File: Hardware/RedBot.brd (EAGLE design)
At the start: 94 x 49.5 mm, 53 parts, among them IC1 FT232RLSSOP, J1 5.5x2.1mm Barrel, J2 AVR_SPI_PRG_6PTH, U1 ATMEGA328P, U2 TB6612FNG, U3 MIC5219 5V, U4 MIC5219 3.3V, X1 USB-B, Y1 16MHz

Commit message: v01 files as sent to protos
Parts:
- removed J1: 5.5x2.1mm Barrel, SparkFun-Connectors:POWER_JACK_SMD
- removed J2: AVR_SPI_PRG_6PTH, SparkFun-Connectors:2X3
- removed X1: USB-B, SparkFun-Connectors:USB-B-PTH
- added JP13: (no value), SparkFun-Connectors:2X3_SMT_POSTS
- added SFE-LOGO1: LOGO-SFENEW, SparkFun-Aesthetics:SFE-NEW-WEBLOGO
- added STANDOFF1, STANDOFF2, STANDOFF3, STANDOFF4: STAND-OFF, SparkFun-Electromechanical:STAND-OFF
- added U$17: OSHW-LOGOS, SparkFun-Aesthetics:OSHW-LOGO-S
- JP3: value STAND-OFF -> 5.5x2.1mm Barrel; device SparkFun-Electromechanical:STAND-OFF -> SparkFun-Connectors:POWER_JACK_SMD
- JP4: value STAND-OFF -> USB-B; device SparkFun-Electromechanical:STAND-OFF -> SparkFun-Connectors:USB-MINIB
- JP5: value STAND-OFF -> AVR_SPI_PRG_6PTH; device SparkFun-Electromechanical:STAND-OFF -> SparkFun-Connectors:2X3
- JP6: value STAND-OFF -> M05X2PTH; device SparkFun-Electromechanical:STAND-OFF -> SparkFun-Connectors:AVR_ICSP
- JP7: value (none) -> M05X2PTH; device SparkFun-Connectors:2X3_SMT_POSTS -> SparkFun-Connectors:AVR_ICSP
- moved JP4 91.2 mm to (88.9, 16.5), turned to 180 degrees
- moved JP3 88.5 mm to (3.81, 15.2)
- moved JP5 71.9 mm to (69.8, 27.9), turned to 90 degrees
- moved JP11 69.3 mm to (12.7, 30.5)
- moved JP9 55.9 mm to (68.6, 40.6)
- moved JP8 43.2 mm to (25.4, 40.6)
- moved JP7 23.7 mm to (2.54, 34.3), turned to 180 degrees
- moved JP6 12.7 mm to (91.4, 34.3)
- moved JP10 10.2 mm to (12.7, 40.6)
- moved JP12 10.2 mm to (81.3, 40.6)
- moved FRAME1 8.13 mm to (-26.7, -16.5)
- renumbered IC1 to U5
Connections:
- new net N$6: JP4.MTN1, JP4.MTN2, JP4.MTN3, JP4.MTN4
- net 5V: now also JP13.3, JP13.4, JP5.2, JP6.1, JP6.3, JP6.5, JP6.7, JP6.9, JP7.1, JP7.3, JP7.5, JP7.7, JP7.9; no longer J2.2, JP9.3, JP9.4
- net GND: now also JP13.5, JP13.6, JP3.P$4, JP4.GND, JP5.6, JP6.10, JP6.2, JP6.4, JP6.6, JP6.8, JP7.10, JP7.2, JP7.4, JP7.8; no longer J1.P$4, J2.6, JP7.5, X1.GND
- net MISO: now also JP5.1; no longer J2.1
- net N$26: now also JP4.D-; no longer X1.D-
- net N$27: now also JP4.D+; no longer X1.D+
- net RESET: now also JP5.5; no longer J2.5
- net SCK: now also JP5.3; no longer J2.3
- net SENSOR_0/SW_TXO: now also JP10.1; no longer JP9.1
- net SENSOR_1/SW_RXI: now also JP10.2; no longer JP9.2
- net SENSOR_2: now also JP11.1; no longer JP10.1
- net SENSOR_3: now also JP11.2; no longer JP10.2
- net SENSOR_4: now also JP12.1; no longer JP11.1
- net SENSOR_5: now also JP12.2; no longer JP11.2
- net SENSOR_6: now also JP13.1; no longer JP12.1
- net SENSOR_7: now also JP13.2; no longer JP12.2
- net SERVO_1: now also JP8.1; no longer JP7.1
- net SERVO_2: now also JP8.2; no longer JP7.2
- net SERVO_3: now also JP9.1; no longer JP8.1
- net SERVO_4/MOSI: now also JP5.4, JP9.2; no longer J2.4, JP8.2
- net V_BATT: now also JP3.VIN0, JP9.3, JP9.4; no longer J1.VIN0, JP7.3, JP7.4
- net V_USB: now also JP4.VBUS; no longer X1.VBUS
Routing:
- net V_USB: track 46.9 -> 36.5 mm, vias 0 -> 2
- net N$27: track 18.1 -> 20.8 mm, vias 0 -> 2
- net N$26: track 14.8 -> 17.1 mm
- net GND: track 77.1 -> 79.2 mm, vias 43 -> 44
- added copper zone on layer 1, net N$6
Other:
- board text added: "M. Hord"
- board text added: "POW"
- board text added: "RedBot"

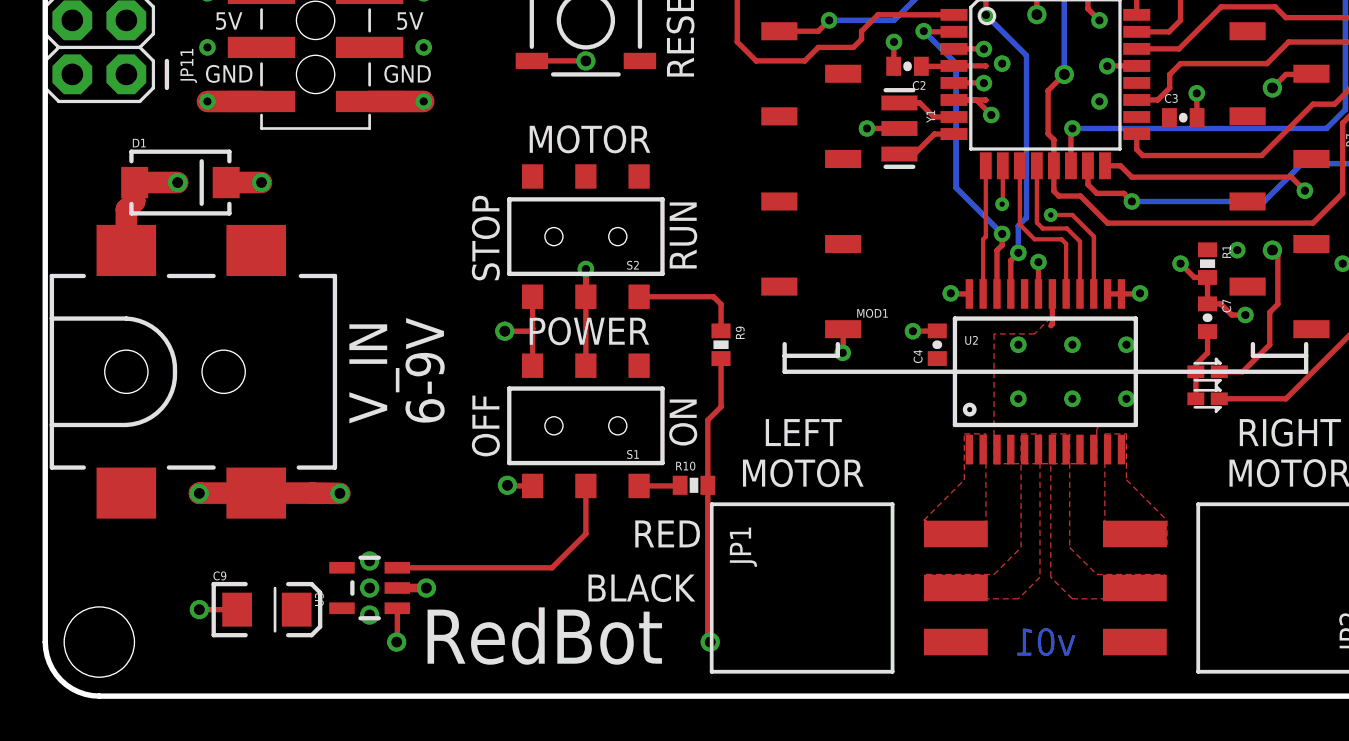
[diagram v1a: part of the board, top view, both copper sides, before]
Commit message: v02 hardware file commit
Initial protos are messed up- no internal copper layers.
Took this opportunity to add a couple of new features:
- .1" headers for input voltage and motor connections
- PMOS switch to disconnect servos when powered down
- fixed barrel jack so the right pin is to ground
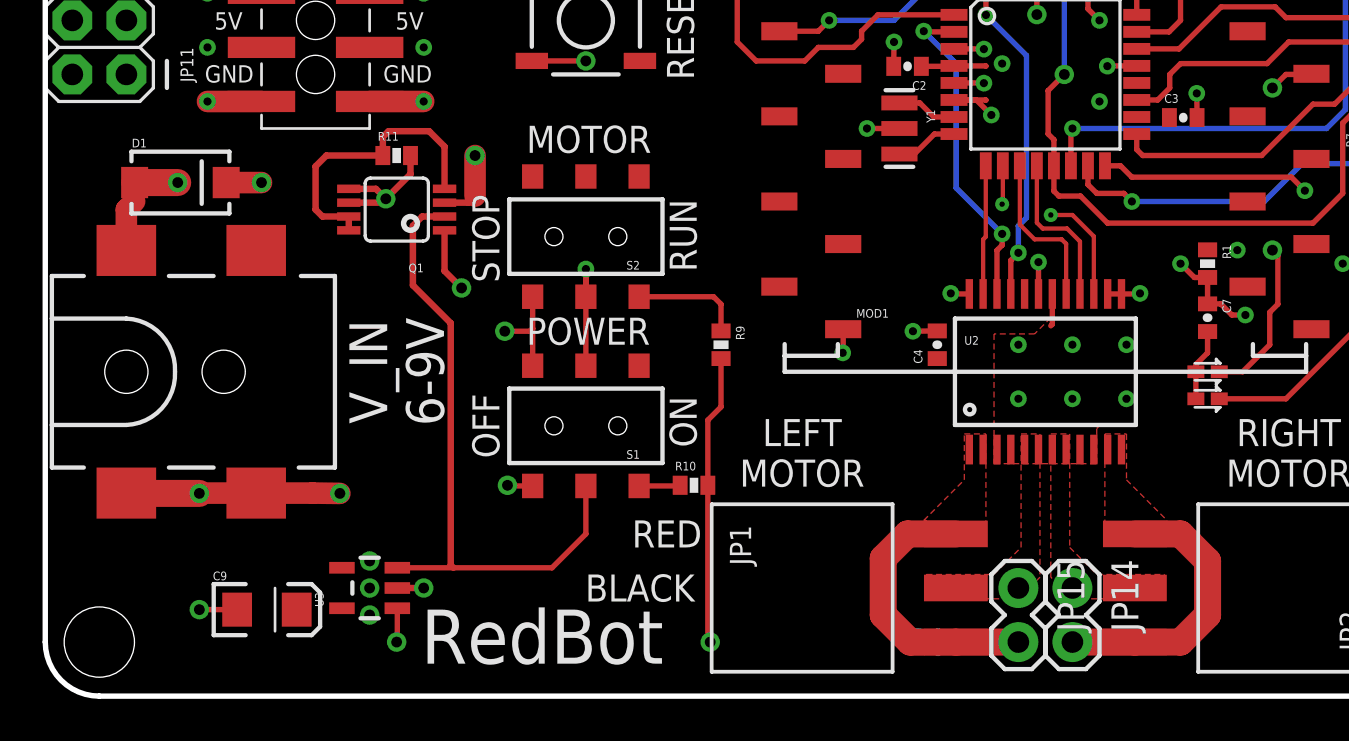
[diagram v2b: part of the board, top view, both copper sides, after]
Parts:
- added JP14, JP15: (no value), SparkFun-Connectors:1X02
- added Q1: (no value), SparkFun-DiscreteSemi:MSOP8
- added R11: 10k, SparkFun-Resistors:0402-RES
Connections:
- new net N$2: Q1.4, Q1.7, Q1.8, R11.1
- new net V_GATED: JP8.3, JP8.4, JP9.3, JP9.4, Q1.3
- net GND: now also JP3.GND, Q1.1
- net L01: now also JP1.3, JP15.2
- net L02: now also JP15.1
- net PROGRAM_ENABLE: now also Q1.2
- net R01: now also JP14.2, JP2.1
- net R02: now also JP14.1
- net V_BATT: now also Q1.5, Q1.6, R11.2; no longer JP8.3, JP8.4, JP9.3, JP9.4
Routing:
- net V_BATT: track 191.0 -> 72.3 mm, vias 7 -> 4
- net V_GATED: track 0.00 -> 113.8 mm, vias 0 -> 5
- net PROGRAM_ENABLE: track 11.8 -> 30.3 mm
- net N$2: track 0.00 -> 13.9 mm
- net L01: track 0.00 -> 13.4 mm
- net R01: track 0.00 -> 13.4 mm
- net GND: track 79.2 -> 85.5 mm, vias 44 -> 45
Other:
- board text added: "v02"
- board text removed: "v01"

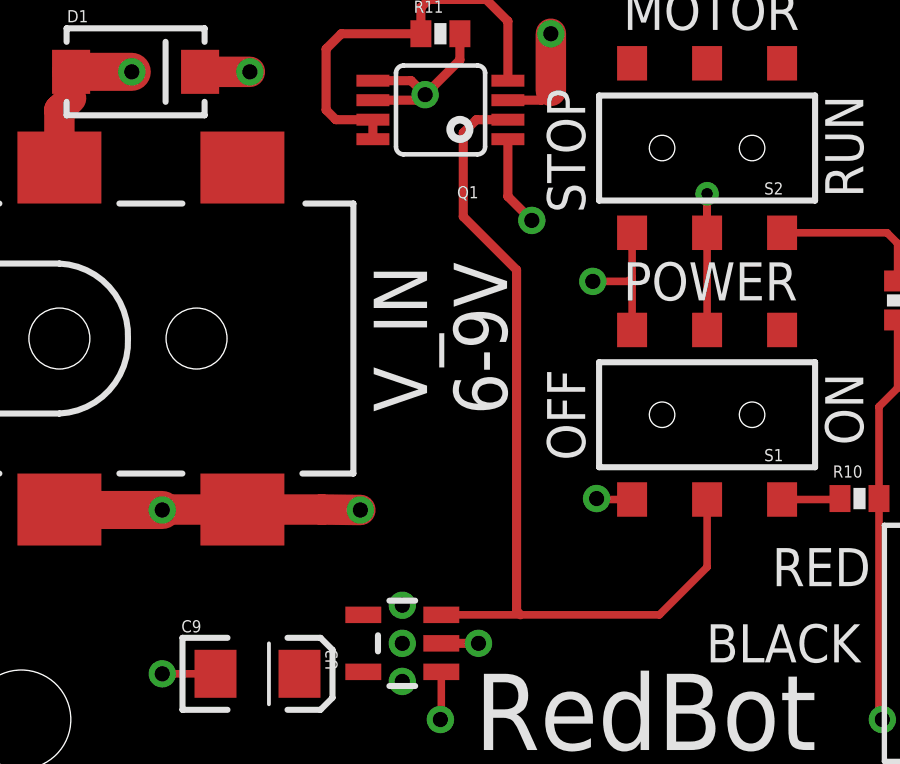
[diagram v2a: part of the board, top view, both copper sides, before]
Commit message: Last commit incomplete; this adds header for PS
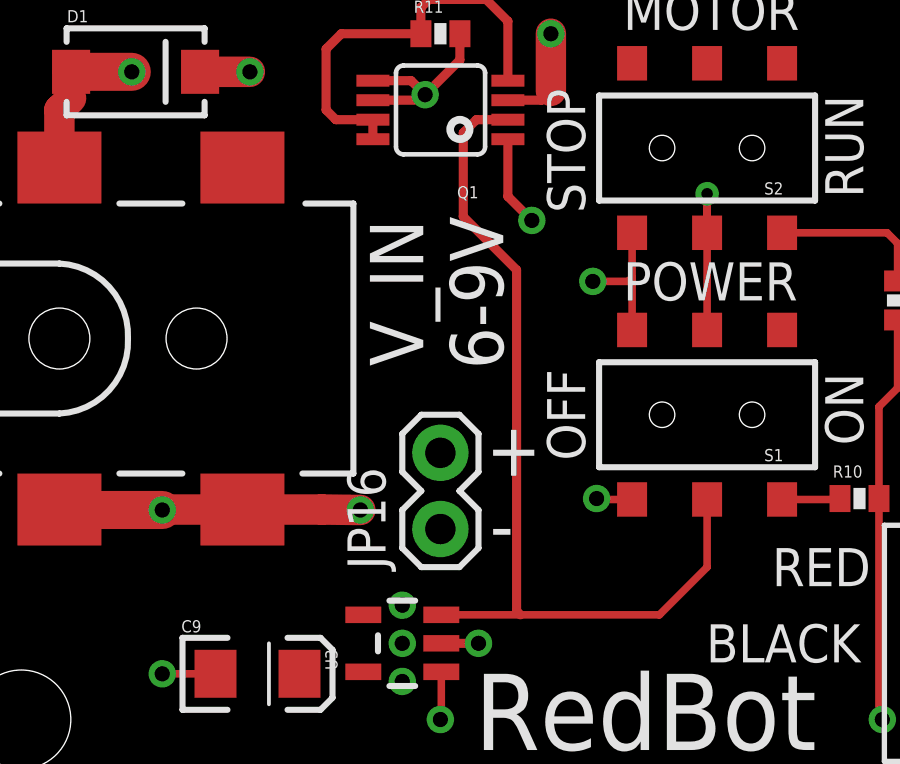
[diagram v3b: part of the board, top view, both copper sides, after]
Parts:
- added JP16: (no value), SparkFun-Connectors:1X02
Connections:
- net GND: now also JP16.1
- net V_BATT: now also JP16.2
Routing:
- net V_BATT: track 72.3 -> 79.9 mm
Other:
- board text added: "+"
- board text added: "-"
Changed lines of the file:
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@@
 <layers>
 <layer number="1" name="Top" color="4" fill="1" visible="yes" active="yes"/>
-<layer number="2" name="5V" color="1" fill="3" visible="no" active="yes"/>
-<layer number="15" name="Gnd" color="4" fill="6" visible="no" active="yes"/>
+<layer number="2" name="5V" color="1" fill="3" visible="yes" active="yes"/>
+<layer number="15" name="Gnd" color="4" fill="6" visible="yes" active="yes"/>
 <layer number="16" name="Bottom" color="1" fill="1" visible="yes" active="yes"/>
 <layer number="17" name="Pads" color="2" fill="1" visible="yes" active="yes"/>
@@
 <text x="42.037" y="48.387" size="0.8128" layer="21" font="vector" ratio="15">XBEE HW SERIAL</text>
 <text x="42.037" y="39.751" size="0.8128" layer="21" font="vector" ratio="15">XBEE SW SERIAL</text>
-<text x="16.51" y="15.24" size="1.778" layer="21" font="vector" ratio="15" rot="R90" align="center">V_IN
+<text x="16.383" y="16.764" size="1.778" layer="21" font="vector" ratio="15" rot="R90" align="center">V_IN
 6-9V</text>
 <text x="78.486" y="16.51" size="0.8128" layer="21" font="vector" ratio="15" align="center">TX</text>
@@
 <text x="71.755" y="41.529" size="0.8128" layer="21" font="vector" ratio="15">POW</text>
 <text x="3.81" y="-16.51" size="1.778" layer="27" font="vector" ratio="15">M. Hord</text>
+<text x="18.034" y="10.668" size="1.778" layer="21" font="vector" ratio="15">+</text>
+<text x="18.161" y="8.128" size="1.778" layer="21" font="vector" ratio="15">-</text>
 </plain>
 <attributes>
@@
 <attribute name="VALUE" value="10k" x="16.51" y="25.4" size="1.778" layer="27" font="vector" ratio="15" display="off"/>
 </element>
+<element name="JP16" library="SparkFun-Connectors" package="1X02" value="" x="16.51" y="8.89" rot="R90"/>
 </elements>
 <signals>
@@
 <wire x1="18.76" y1="19.975" x2="19.558" y2="19.177" width="0.3048" layer="1"/>
 <via x="19.558" y="19.177" extent="1-16" drill="0.508"/>
+<contactref element="JP16" pad="1"/>
 </signal>
 <signal name="SENSOR_0/SW_TXO">
@@
 <wire x1="17.16" y1="24.526" x2="16.002" y2="23.368" width="0.3048" layer="1"/>
 <wire x1="4.2" y1="24.13" x2="4.2" y2="23.25" width="0.3048" layer="1"/>
+<contactref element="JP16" pad="2"/>
+<wire x1="16.51" y1="11.43" x2="16.51" y2="19.05" width="1.016" layer="15"/>
 </signal>
 <signal name="N$23">

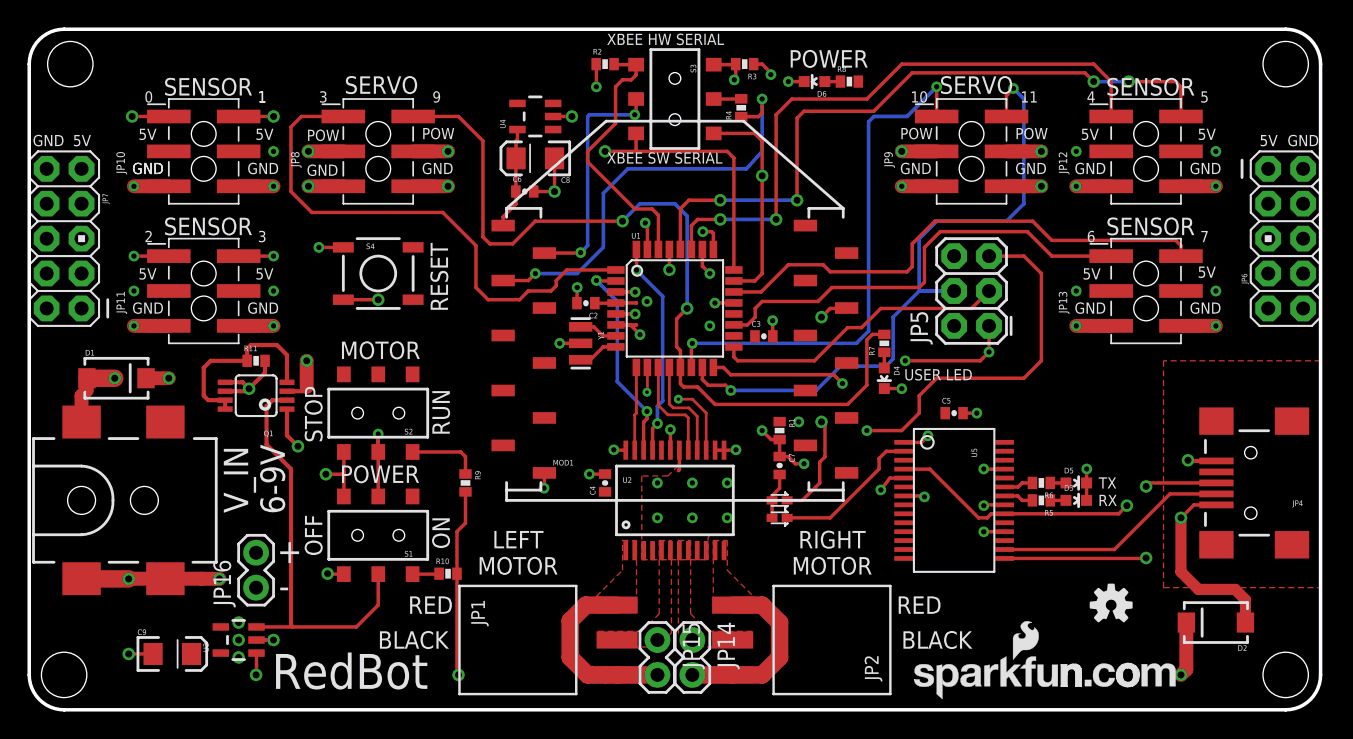
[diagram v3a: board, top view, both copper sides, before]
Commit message: Changes from v01 Changed top plane to ground Fixed issue with barrel jack connection Add .1" header for power input by barrel jack Add PMOSFET power switch for servo motors
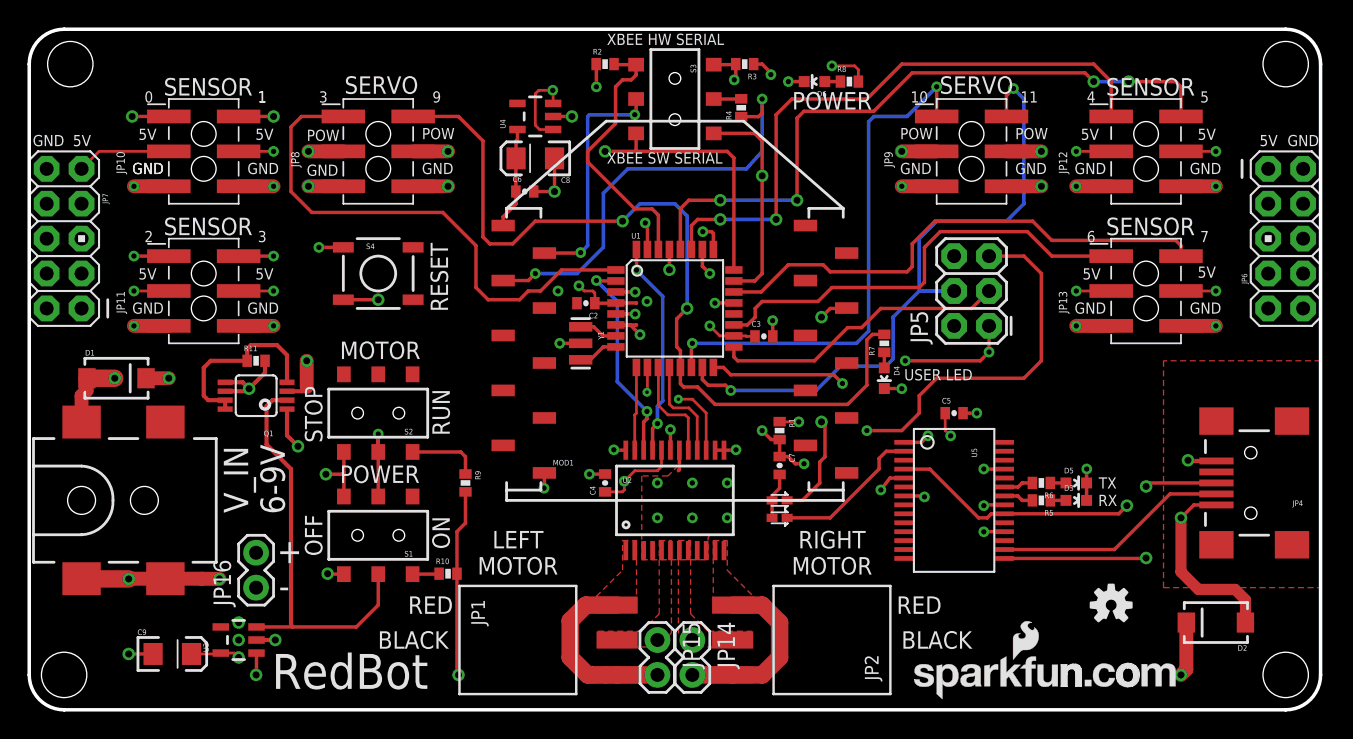
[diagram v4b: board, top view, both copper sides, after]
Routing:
- net 5V: track 6.60 -> 59.2 mm, vias 14 -> 19
- net V_IN: track 114.6 -> 118.8 mm
- net FT232_RXI: track 42.4 -> 43.4 mm
- net GND: track 85.5 -> 84.5 mm
- removed copper zone on layer 1, net 5V
